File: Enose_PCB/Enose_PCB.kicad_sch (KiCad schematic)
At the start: 15 parts, among them J1 B4B-XH-A_LF__SN_, J2 B4B-XH-A_LF__SN_, J3 B4B-XH-A_LF__SN_, J4 DA15_Pins, SW1 SW_DPST_x2, SW2 SW_DPST_x2, U1 ESP32-S3-WROOM-1

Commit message: adding fan power to main pcb
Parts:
- added C25: 100n, symbol Device:C
- added J10: Fan, Connector_PinHeader_2.54mm:PinHeader_1x02_P2.54mm_Vertical, symbol Connector:Conn_01x02_Pin
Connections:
- net +3V3: now also C25.2, J10.1 (Pin_1)
- net GND: now also C25.1, J10.2 (Pin_2)
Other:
- note added: "Fan Power"

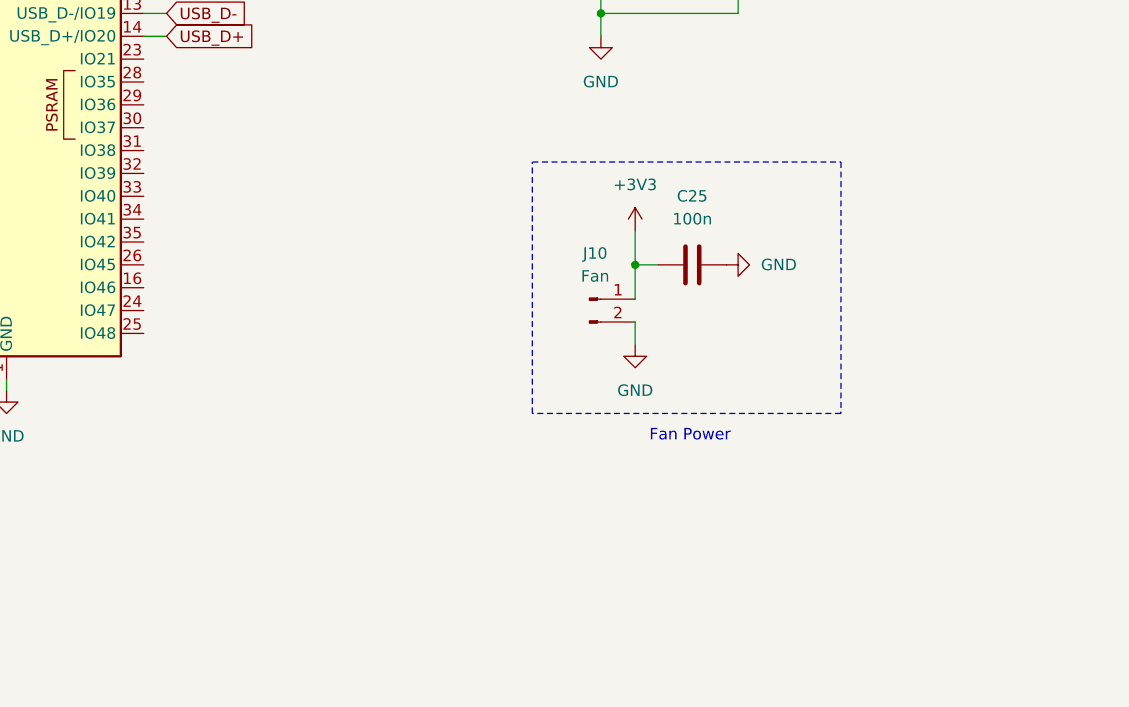
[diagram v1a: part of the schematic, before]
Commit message: adding fan control circuitry
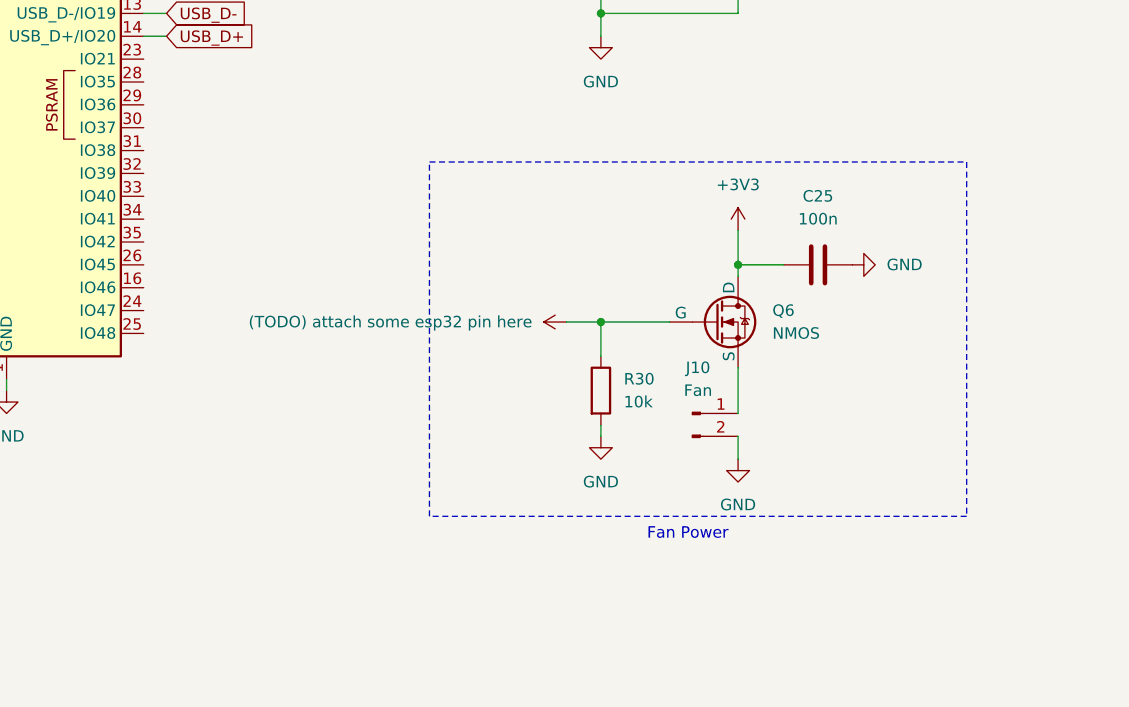
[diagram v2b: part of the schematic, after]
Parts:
- added Q6: NMOS, Ventsi_Lib:Ventsi_SOT23, symbol Simulation_SPICE:NMOS
- added R30: 10k, Resistor_SMD:R_0805_2012Metric_Pad1.20x1.40mm_HandSolder, symbol Device:R
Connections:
- net +3V3: now also Q6.1 (D); no longer J10.1 (Pin_1)
- net GND: now also R30.2
- new net: J10.1 (Pin_1), Q6.3 (S)
- new net (TODO) attach some esp32 pin here: Q6.2 (G), R30.1
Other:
- moved on the sheet: C25, J10

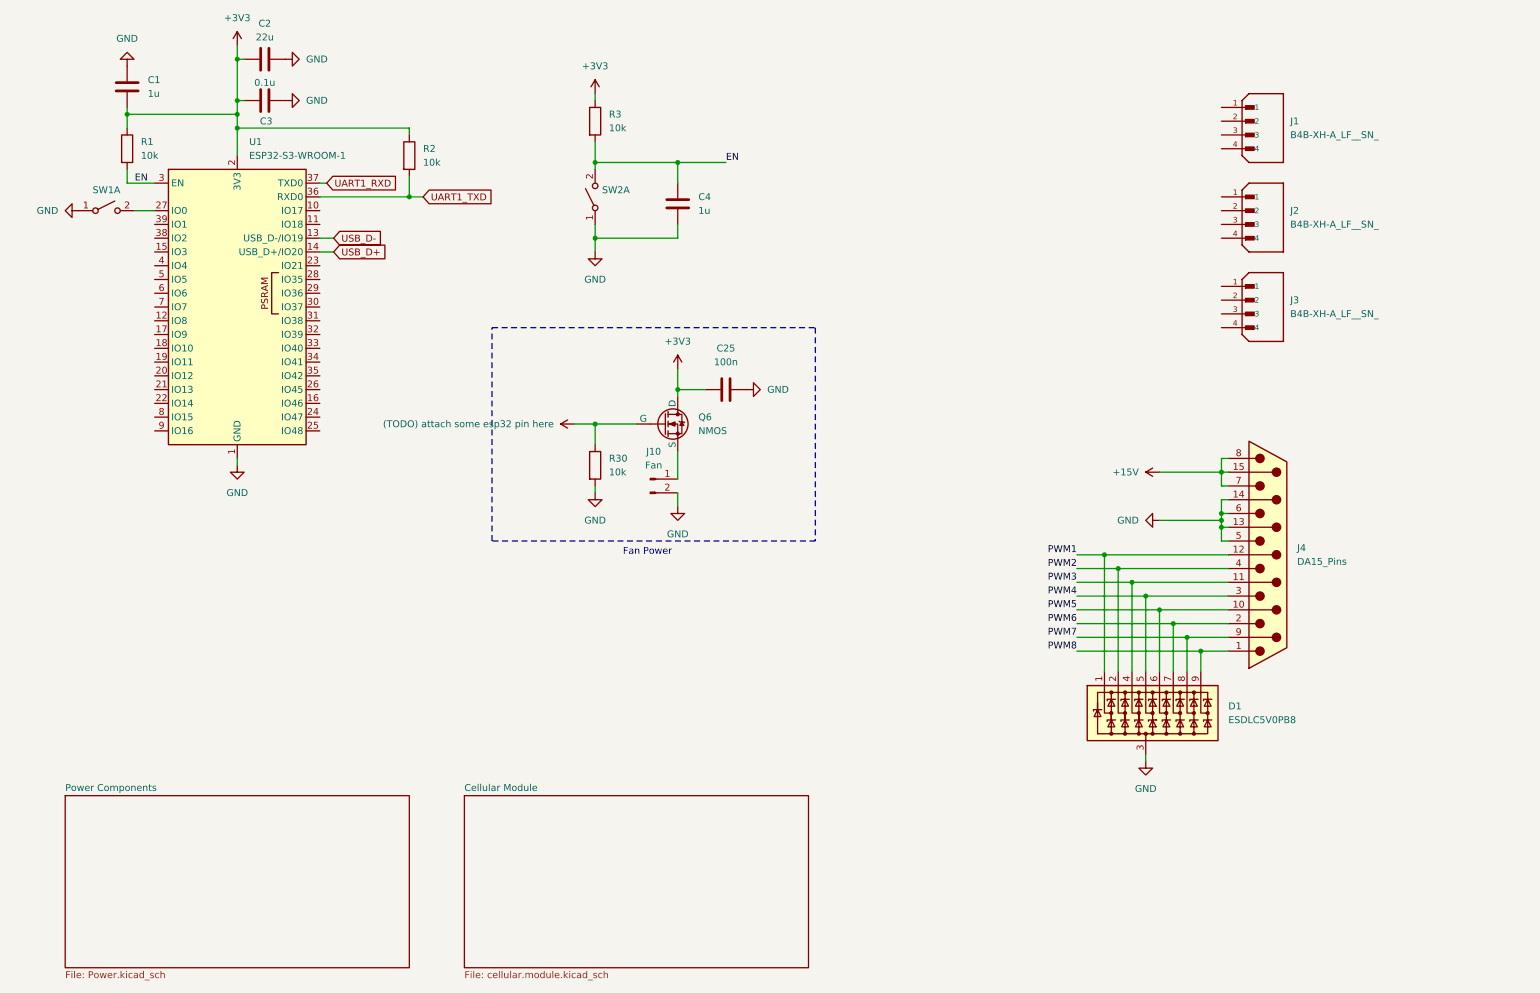
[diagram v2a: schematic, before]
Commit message: assigning gpi06 to control fan
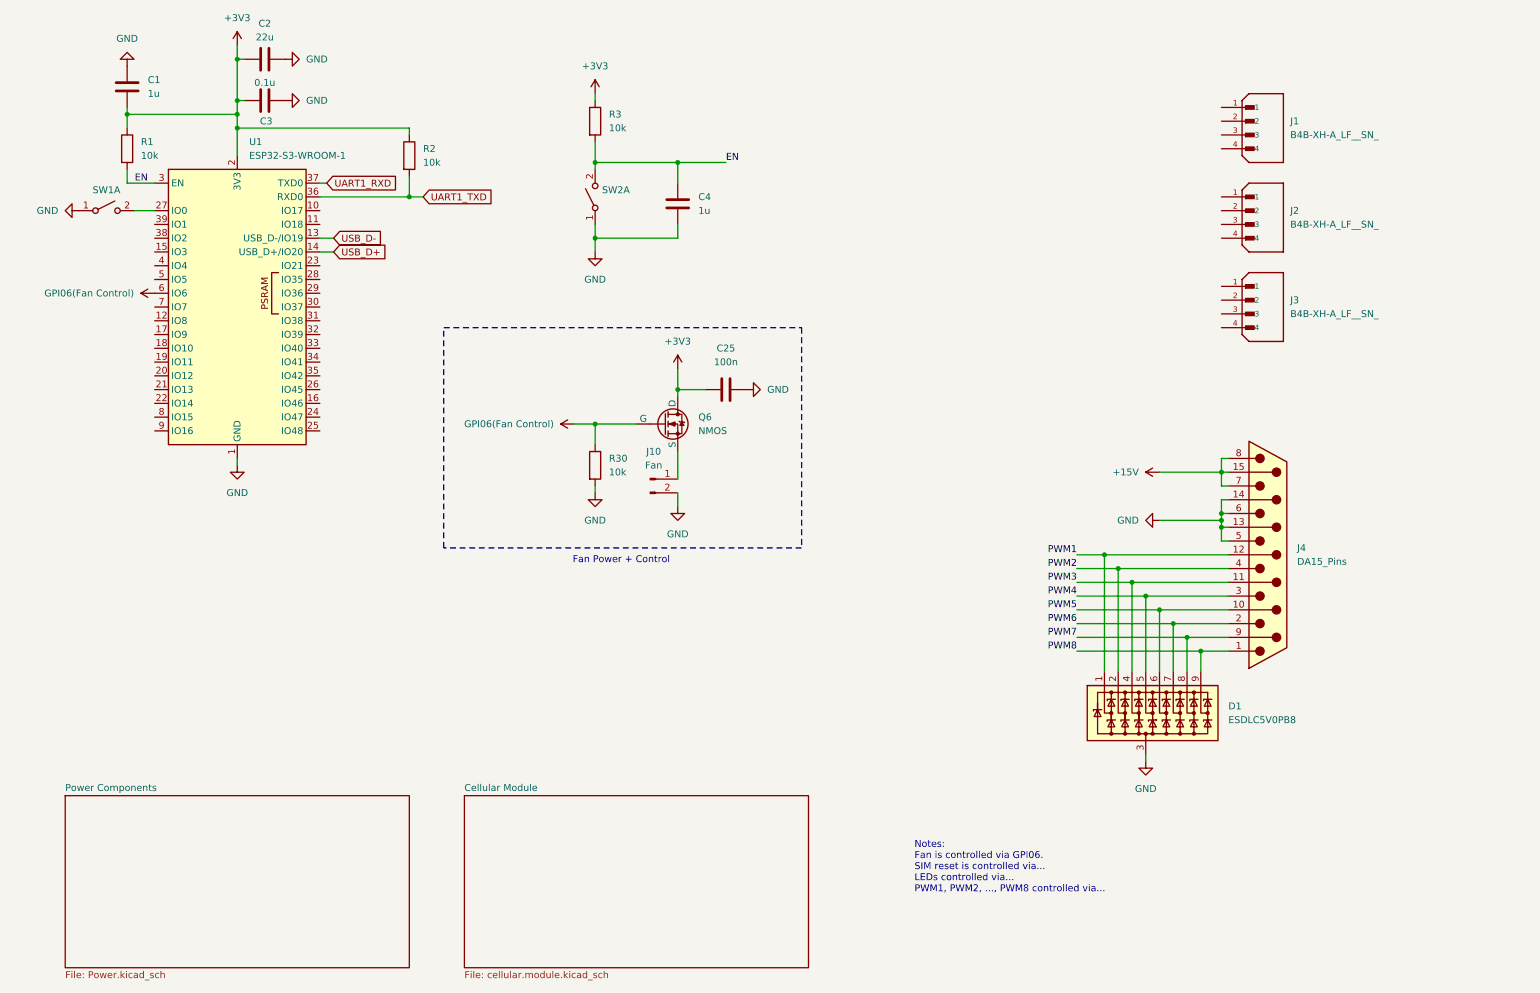
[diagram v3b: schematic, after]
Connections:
- net (TODO) attach some esp32 pin here is gone; now on net GPI06(Fan Control): Q6.2 (G), R30.1
- net GPI06(Fan Control): now reaches U1.6 (IO6)
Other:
- note added: "Fan Power + Control"
- note added: "Notes: Fan is controlled via GPI06. SIM reset is controlled via... LEDs controlled via... PWM1, PWM2, ..., PWM8 controlled via..."
- note removed: "Fan Power"
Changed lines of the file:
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@@
 	(paper "A4")
 	(rectangle
-		(start 100.33 72.39)
-		(end 160.02 111.76)
+		(start 91.44 72.39)
+		(end 157.48 113.03)
 		(stroke
 			(width 0)
@@
 		)
 	)
-	(text "Fan Power"
+	(text "Notes:\nFan is controlled via GPI06.\nSIM reset is controlled via...\nLEDs controlled via...\nPWM1, PWM2, ..., PWM8 controlled via..."
 		(exclude_from_sim no)
-		(at 129.032 113.792 0)
+		(at 178.308 171.958 0)
+		(effects
+			(font
+				(size 1.27 1.27)
+			)
+			(justify left)
+		)
+	)
+	(text "Fan Power + Control"
+		(exclude_from_sim no)
+		(at 124.206 115.316 0)
 		(effects
 			(font
@@
 	)
 	(symbol
+		(lib_id "power:+3V3")
+		(at 115.57 90.17 90)
+		(unit 1)
+		(exclude_from_sim no)
+		(in_bom yes)
+		(on_board yes)
+		(dnp no)
+		(fields_autoplaced yes)
+		(property "Reference" "#PWR069"
+			(at 119.38 90.17 0)
+			(effects
+				(font
+					(size 1.27 1.27)
+				)
+				(hide yes)
+			)
+		)
+		(property "Value" "GPI06(Fan Control)"
+			(at 111.76 90.1699 90)
+			(effects
+				(font
+					(size 1.27 1.27)
+				)
+				(justify left)
+			)
+		)
+		(property "Footprint" ""
+			(at 115.57 90.17 0)
+			(effects
+				(font
+					(size 1.27 1.27)
+				)
+				(hide yes)
+			)
+		)
+		(property "Datasheet" ""
+			(at 115.57 90.17 0)
+			(effects
+				(font
+					(size 1.27 1.27)
+				)
+				(hide yes)
+			)
+		)
+		(property "Description" "Power symbol creates a global label with name \"+3V3\""
+			(at 115.57 90.17 0)
+			(effects
+				(font
+					(size 1.27 1.27)
+				)
+				(hide yes)
+			)
+		)
+		(pin "1"
+		)
+		(instances
+			(project "Enose_PCB"
+				(path "/eef70be0-4107-491c-8ca0-465071a6397e"
+					(reference "#PWR069")
+					(unit 1)
+				)
+			)
+		)
+	)
+	(symbol
 		(lib_id "Device:R")
 		(at 33.02 39.37 0)
@@
 	)
 	(symbol
-		(lib_id "power:+3V3")
-		(at 115.57 90.17 90)
-		(unit 1)
-		(exclude_from_sim no)
-		(in_bom yes)
-		(on_board yes)
-		(dnp no)
-		(fields_autoplaced yes)
-		(property "Reference" "#PWR069"
-			(at 119.38 90.17 0)
-			(effects
-				(font
-					(size 1.27 1.27)
-				)
-				(hide yes)
-			)
-		)
-		(property "Value" "(TODO) attach some esp32 pin here"
-			(at 111.76 90.1699 90)
-			(effects
-				(font
-					(size 1.27 1.27)
-				)
-				(justify left)
-			)
-		)
-		(property "Footprint" ""
-			(at 115.57 90.17 0)
-			(effects
-				(font
-					(size 1.27 1.27)
-				)
-				(hide yes)
-			)
-		)
-		(property "Datasheet" ""
-			(at 115.57 90.17 0)
-			(effects
-				(font
-					(size 1.27 1.27)
-				)
-				(hide yes)
-			)
-		)
-		(property "Description" "Power symbol creates a global label with name \"+3V3\""
-			(at 115.57 90.17 0)
-			(effects
-				(font
-					(size 1.27 1.27)
-				)
-				(hide yes)
-			)
-		)
-		(pin "1"
-		)
-		(instances
-			(project "Enose_PCB"
-				(path "/eef70be0-4107-491c-8ca0-465071a6397e"
-					(reference "#PWR069")
-					(unit 1)
-				)
-			)
-		)
-	)
-	(symbol
 		(lib_id "power:GND")
 		(at 220.98 152.4 0)
@@
 					(unit 1)
 				)
+			)
+		)
+	)
+	(symbol
+		(lib_id "power:+3V3")
+		(at 38.1 66.04 90)
+		(unit 1)
+		(exclude_from_sim no)
+		(in_bom yes)
+		(on_board yes)
+		(dnp no)
+		(fields_autoplaced yes)
+		(property "Reference" "#PWR070"
+			(at 41.91 66.04 0)
+			(effects
+				(font
+					(size 1.27 1.27)
+				)
+				(hide yes)
+			)
+		)
+		(property "Value" "GPI06(Fan Control)"
+			(at 34.29 66.0399 90)
+			(effects
+				(font
+					(size 1.27 1.27)
+				)
+				(justify left)
+			)
+		)
+		(property "Footprint" ""
+			(at 38.1 66.04 0)
+			(effects
+				(font
+					(size 1.27 1.27)
+				)
+				(hide yes)
+			)
+		)
+		(property "Datasheet" ""
+			(at 38.1 66.04 0)
+			(effects
+				(font
+					(size 1.27 1.27)
+				)
+				(hide yes)
+			)
+		)
+		(property "Description" "Power symbol creates a global label with name \"+3V3\""
+			(at 38.1 66.04 0)
+			(effects
+				(font
+					(size 1.27 1.27)
+				)
+				(hide yes)
+			)
+		)
+		(pin "1"
+		)
+		(instances
+			(project "Enose_PCB"
+				(path "/eef70be0-4107-491c-8ca0-465071a6397e"
+					(reference "#PWR070")
+					(unit 1)
+				)

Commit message: Added LED
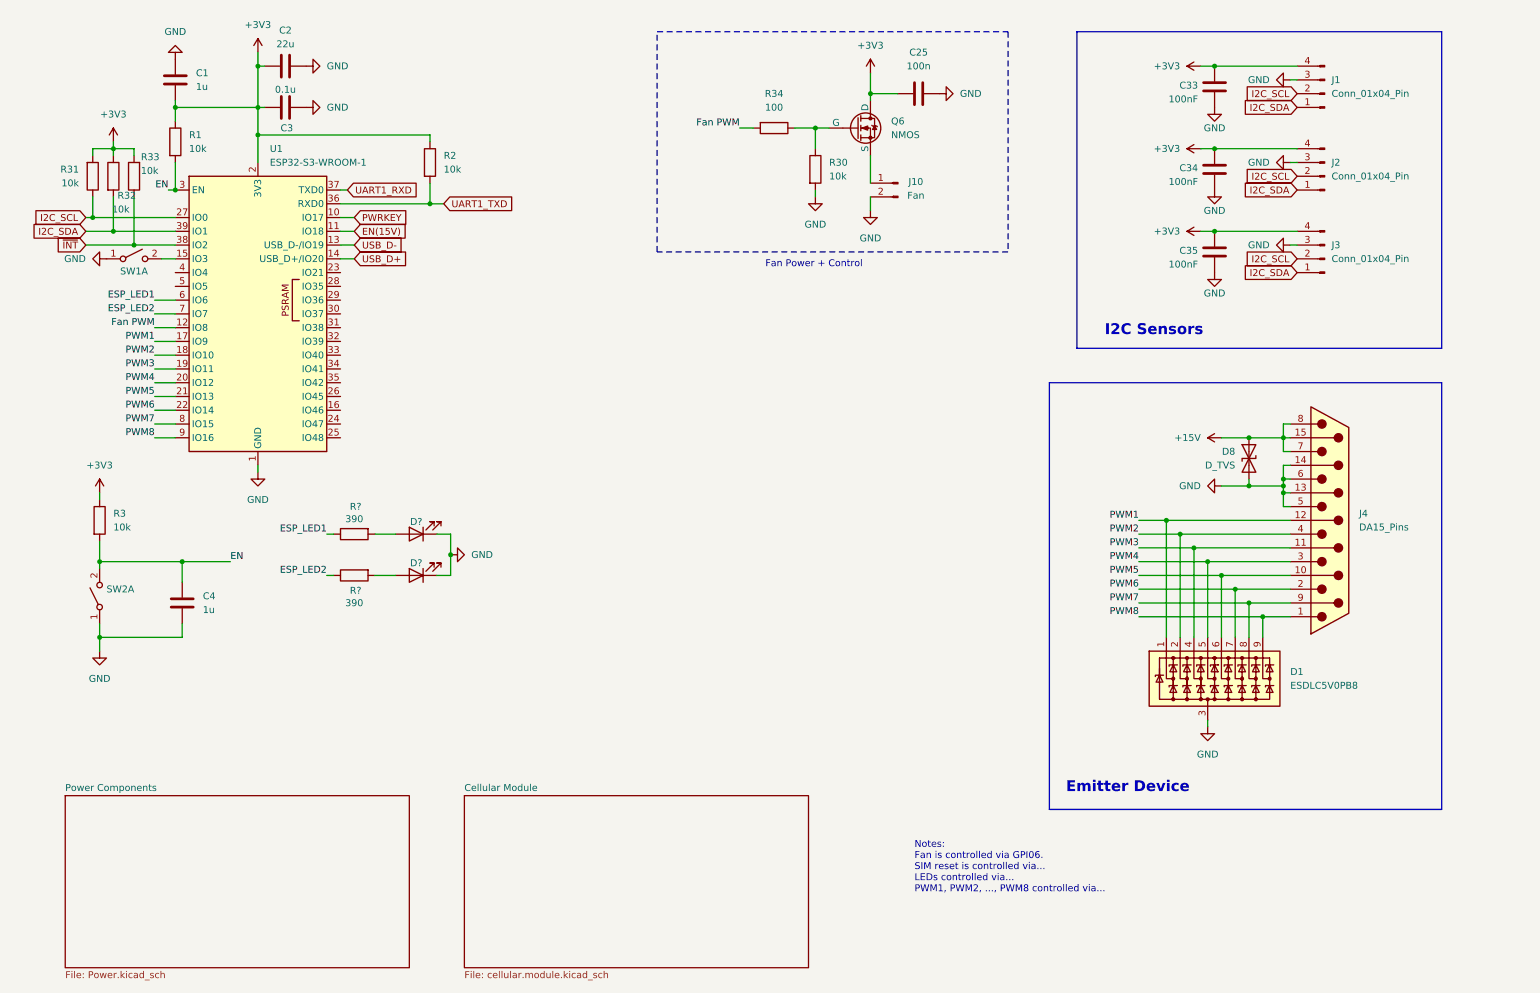
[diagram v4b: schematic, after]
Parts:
- removed J1, J2, J3: B4B-XH-A_LF__SN_, B4B-XH-A_LF__SN_:JST_B4B-XH-A_LF__SN_, symbol B4B-XH-A_LF__SN_:B4B-XH-A_LF__SN_
- added C33, C34, C35: 100nF, symbol Device:C
- added D8: D_TVS, symbol Device:D_TVS
- added D? (x2): LED Amber, symbol Device:LED
- added J1, J2, J3: Conn_01x04_Pin, symbol Connector:Conn_01x04_Pin
- added R31, R32, R33: 10k, symbol Device:R
- added R34: 100, symbol Device:R
- added R? (x2): 390, symbol Device:R
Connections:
- net +15V: now also D8.1 (A1)
- net +3V3: now also C33.1, C34.1, C35.1, J1.4 (Pin_4), J2.4 (Pin_4), J3.4 (Pin_4), R31.2, R32.1, R33.2
- net GND: now also C33.2, C34.2, C35.2, D8.2 (A2), D?.1 (K), D?.1 (K), J1.3 (Pin_3), J2.3 (Pin_3), J3.3 (Pin_3)
- net PWM1: now also U1.17 (IO9)
- net PWM2: now also U1.18 (IO10)
- net PWM3: now also U1.19 (IO11)
- net PWM4: now also U1.20 (IO12)
- net PWM5: now also U1.21 (IO13)
- net PWM6: now also U1.22 (IO14)
- net PWM7: now also U1.8 (IO15)
- net PWM8: now also U1.9 (IO16)
- net at SW1.2 (B): now also U1.15 (IO3); no longer U1.27 (IO0)
- net PWRKEY: now reaches U1.10 (IO17)
- net EN(15V): now reaches U1.11 (IO18)
- net Fan PWM: now reaches U1.12 (IO8)
- net Fan PWM: now also R34.2
- net ~{INT}: now reaches U1.38 (IO2)
- net ~{INT}: now also R33.1
- net I2C_SDA: now reaches U1.39 (IO1)
- net I2C_SDA: now also J1.1 (Pin_1), J2.1 (Pin_1), J3.1 (Pin_1), R32.2
- net ESP_LED2: now reaches U1.7 (IO7)
- net ESP_LED2: now also R?.1
- net GPI06(Fan Control): no longer names the net of Q6.2 (G), R30.1
- net GPI06(Fan Control): now also R34.1; no longer U1.6 (IO6)
- new net: D?.2 (A), R?.2 (x2)
- new net ESP_LED1: R?.1, U1.6 (IO6)
- new net I2C_SCL: J1.2 (Pin_2), J2.2 (Pin_2), J3.2 (Pin_2), R31.1, U1.27 (IO0)
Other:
- note added: "Emitter Device"
- note added: "I2C Sensors"
- moved on the sheet: C1, C2, C25, C3, C4, D1, J10, J4, Q6, R1, R2, R3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
